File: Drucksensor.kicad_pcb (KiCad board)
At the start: 2 copper layers, 99 x 67 mm, 95 parts, among them J101 Conn_01x02, J102 Start, J103 RJ45, J104 RJ45, J105 DB15_Female_MountingHoles, J106 Serial, J107 Conn_01x03_Male, Q101 Q_NMOS_GSD, Q102 Q_NMOS_GSD, Q103 Q_NMOS_GSD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

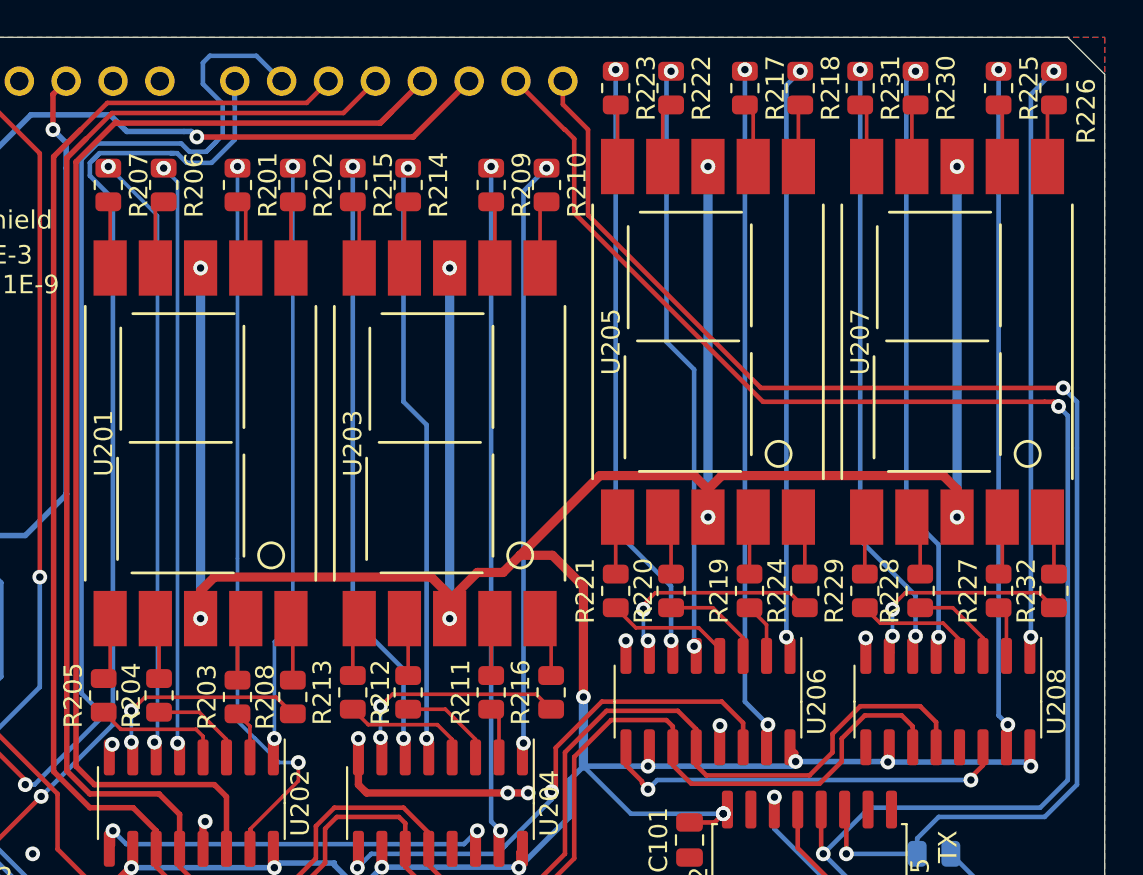
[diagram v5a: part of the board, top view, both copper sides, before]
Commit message: Software-Serial für RS232 interface
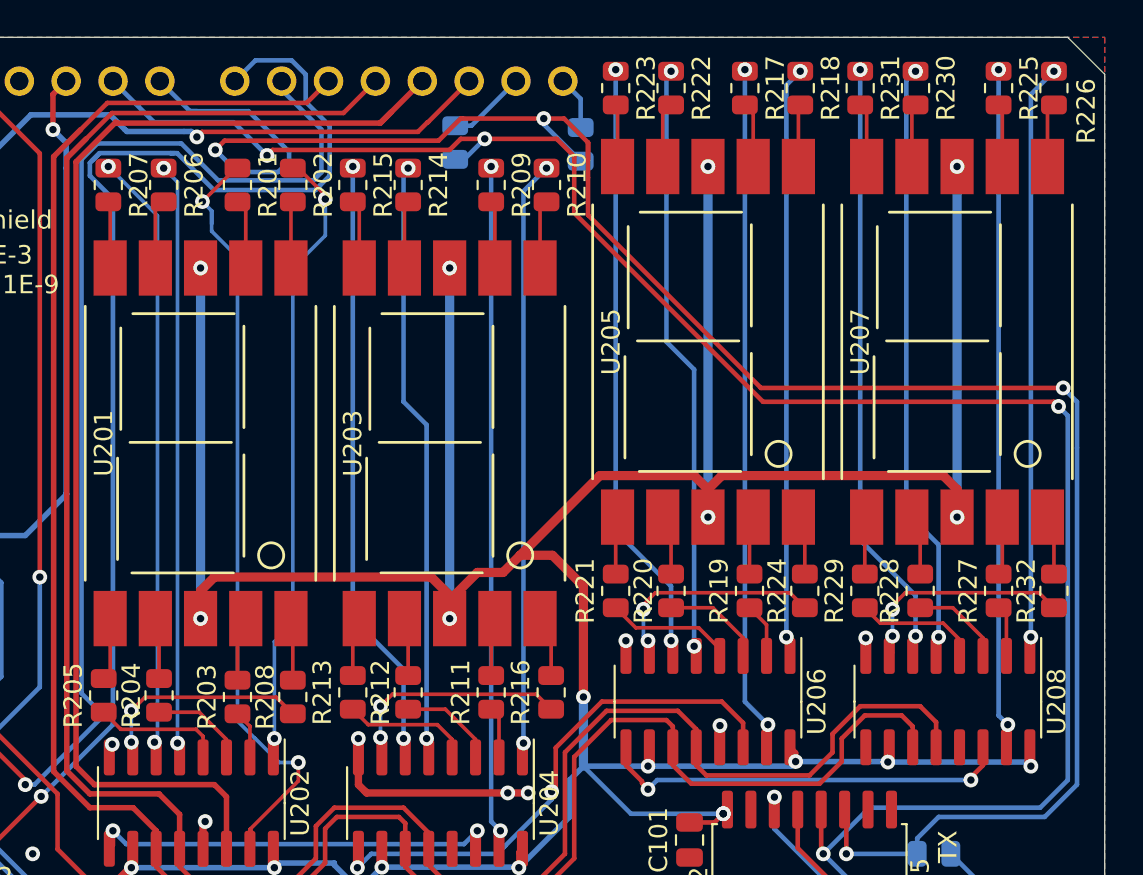
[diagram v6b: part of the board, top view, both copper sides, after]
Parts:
- added R123: Open, Resistor_SMD:R_0805_2012Metric, B.Cu at (119.8, 23.7)
- added R124: Open, Resistor_SMD:R_0805_2012Metric, B.Cu at (126.6, 23.8)
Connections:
- A101 pad 23: unconnected-(A101-Pad23) -> /TX_2
- A101 pad 24: unconnected-(A101-Pad24) -> /RX_2
- R105 pad 2: /TX -> /TX_2
- R116 pad 2: /RX -> /RX_2
- U102 pad 11: /TX -> /TX_2
- U102 pad 12: /RX -> /RX_2
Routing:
- net /TX_2: track 0.00 -> 112.2 mm, vias 0 -> 4
- net /RX_2: track 0.00 -> 107.4 mm, vias 0 -> 4
- net /RX: track 83.3 -> 4.30 mm, vias 2 -> 0
- net /TX: track 76.3 -> 2.92 mm, vias 2 -> 0
- net /Magnetron_Enable: track 61.1 -> 73.2 mm
- net Net-(R201-Pad1): track 41.1 -> 43.4 mm
- net Net-(R202-Pad1): track 32.5 -> 34.2 mm
- net /EnableAll: track 77.7 -> 79.2 mm

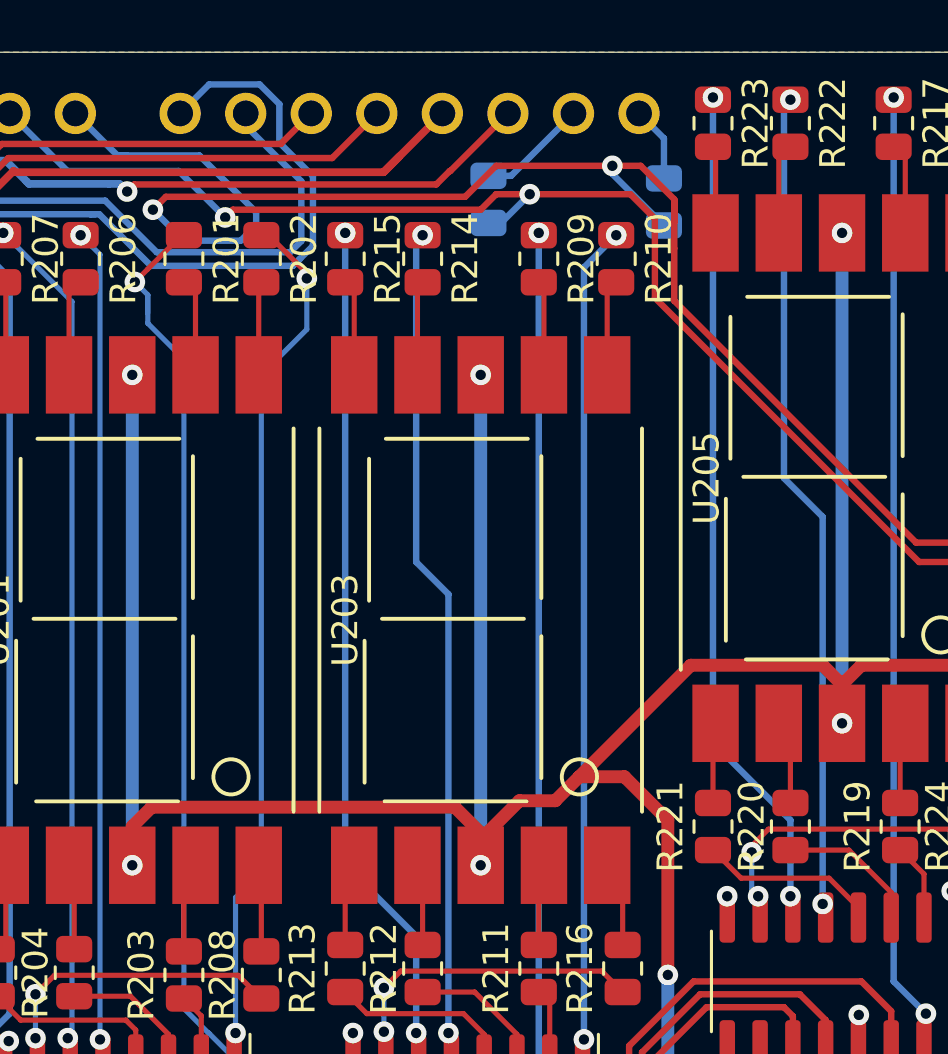
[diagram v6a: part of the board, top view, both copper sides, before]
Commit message: Flächen angepasst
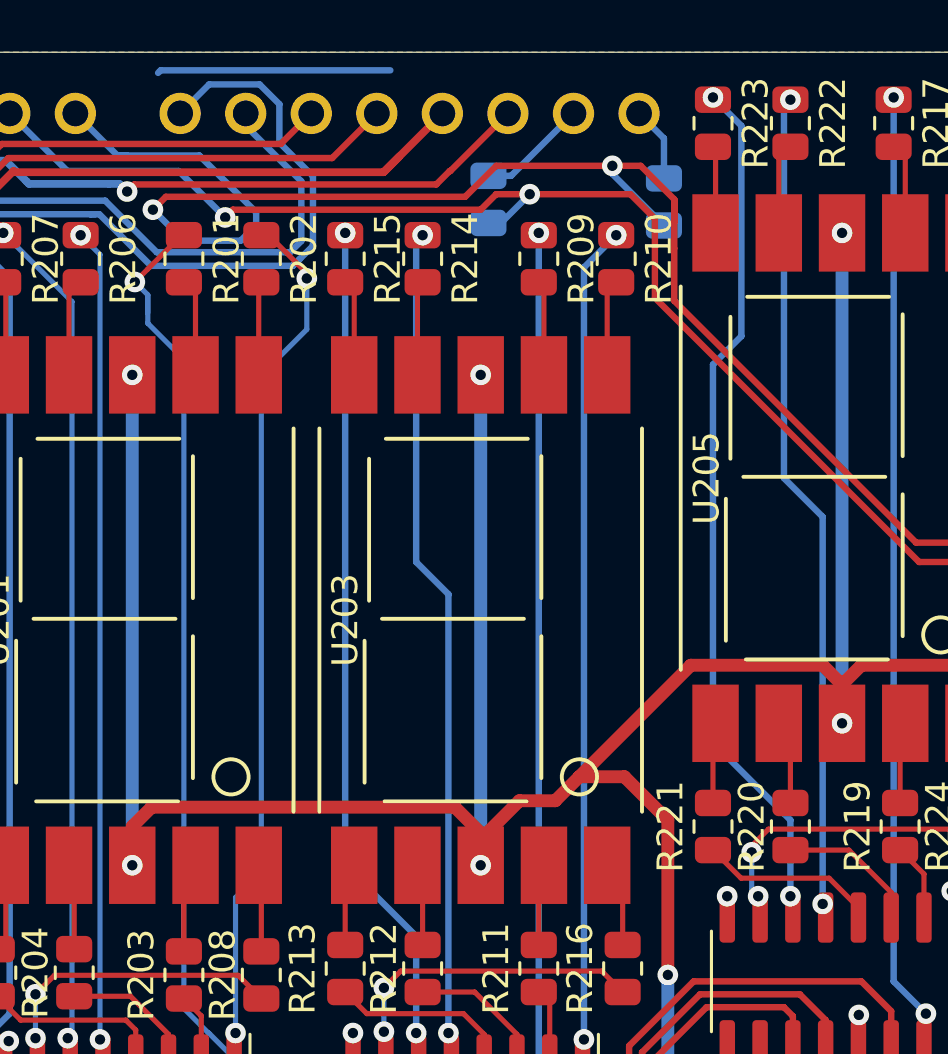
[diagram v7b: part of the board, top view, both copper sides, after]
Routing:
- net GND: track 80.4 -> 89.4 mm
- net Net-(R223-Pad1): track 33.1 -> 34.1 mm
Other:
- board text added: "Bridge for RX/TX_0"
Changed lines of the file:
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@@
     (effects (font (size 2 2) (thickness 0.15)) (justify mirror))
+  )
+  (gr_text "Bridge for RX/TX_0" (at 120.6 26.5) (layer "B.SilkS")
+    (effects (font (size 1 1) (thickness 0.15)) (justify mirror))
   )
   (gr_text "TX RX" (at 154 65.25 90) (layer "B.SilkS")
@@
   (via (at 96.9 62.25) (size 0.8) (drill 0.4) (layers "F.Cu" "B.Cu") (net 12))
   (via (at 82.25 41.25) (size 0.8) (drill 0.4) (layers "F.Cu" "B.Cu") (net 12))
+  (segment (start 116 18.7) (end 107.1 18.7) (width 0.25) (layer "B.Cu") (net 12))
+  (segment (start 107.1 18.7) (end 107 18.8) (width 0.25) (layer "B.Cu") (net 12))
   (segment (start 92.8 63.775) (end 92.8 63.65) (width 0.3) (layer "F.Cu") (net 13))
   (segment (start 94.5 61.95) (end 94.55 61.95) (width 0.25) (layer "F.Cu") (net 13))
@@
   (via (at 128.5 19.75) (size 0.8) (drill 0.4) (layers "F.Cu" "B.Cu") (net 80))
   (via (at 131.5 50.6995) (size 0.8) (drill 0.4) (layers "F.Cu" "B.Cu") (net 80))
-  (segment (start 128.5 19.75) (end 128.5 44.75) (width 0.25) (layer "B.Cu") (net 80))
-  (segment (start 131.5 47.75) (end 131.5 50.6995) (width 0.25) (layer "B.Cu") (net 80))
-  (segment (start 128.5 44.75) (end 131.5 47.75) (width 0.25) (layer "B.Cu") (net 80))
+  (segment (start 129.6 29) (end 129.6 20.85) (width 0.25) (layer "B.Cu") (net 80))
+  (segment (start 129.6 20.85) (end 128.5 19.75) (width 0.25) (layer "B.Cu") (net 80))
+  (segment (start 128.5 44.75) (end 128.5 30.1) (width 0.25) (layer "B.Cu") (net 80))
+  (segment (start 131.5 47.75) (end 128.5 44.75) (width 0.25) (layer "B.Cu") (net 80))
+  (segment (start 131.5 50.6995) (end 131.5 47.75) (width 0.25) (layer "B.Cu") (net 80))
+  (segment (start 128.5 30.1) (end 129.6 29) (width 0.25) (layer "B.Cu") (net 80))
   (segment (start 128.6 21.7625) (end 128.5 21.6625) (width 0.2) (layer "F.Cu") (net 81))
   (segment (start 128.6 25) (end 128.6 21.7625) (width 0.2) (layer "F.Cu") (net 81))

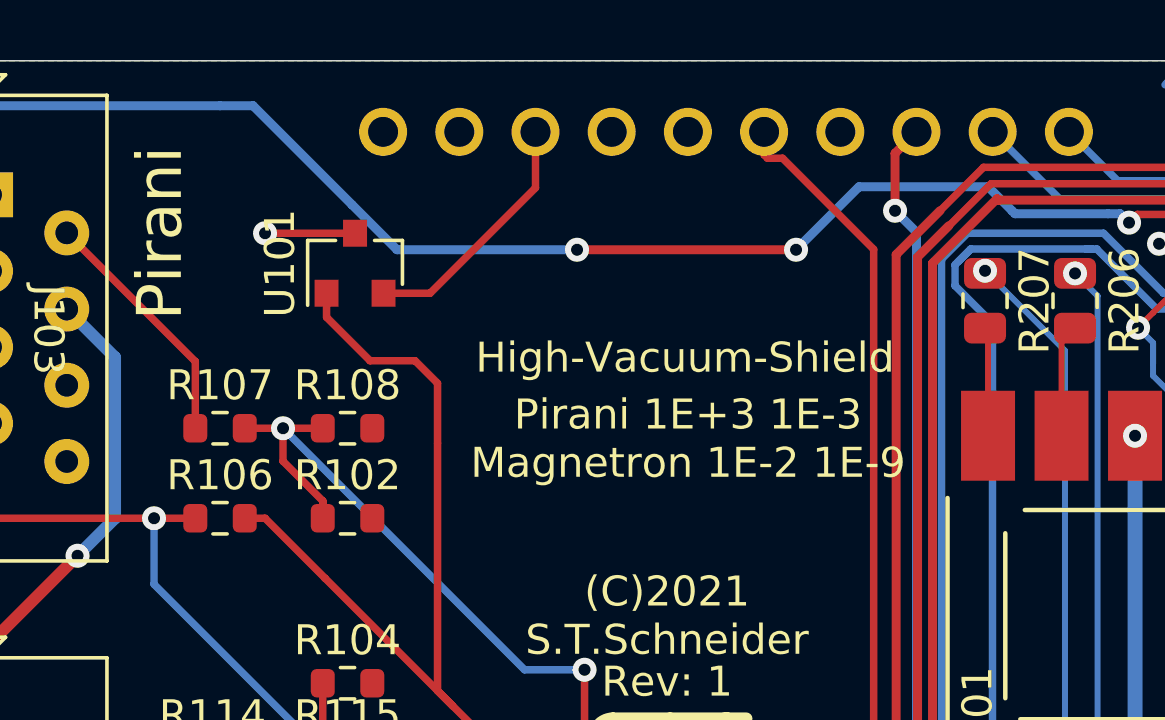
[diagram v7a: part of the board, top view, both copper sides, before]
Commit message: Kondensatoren für V-Ref
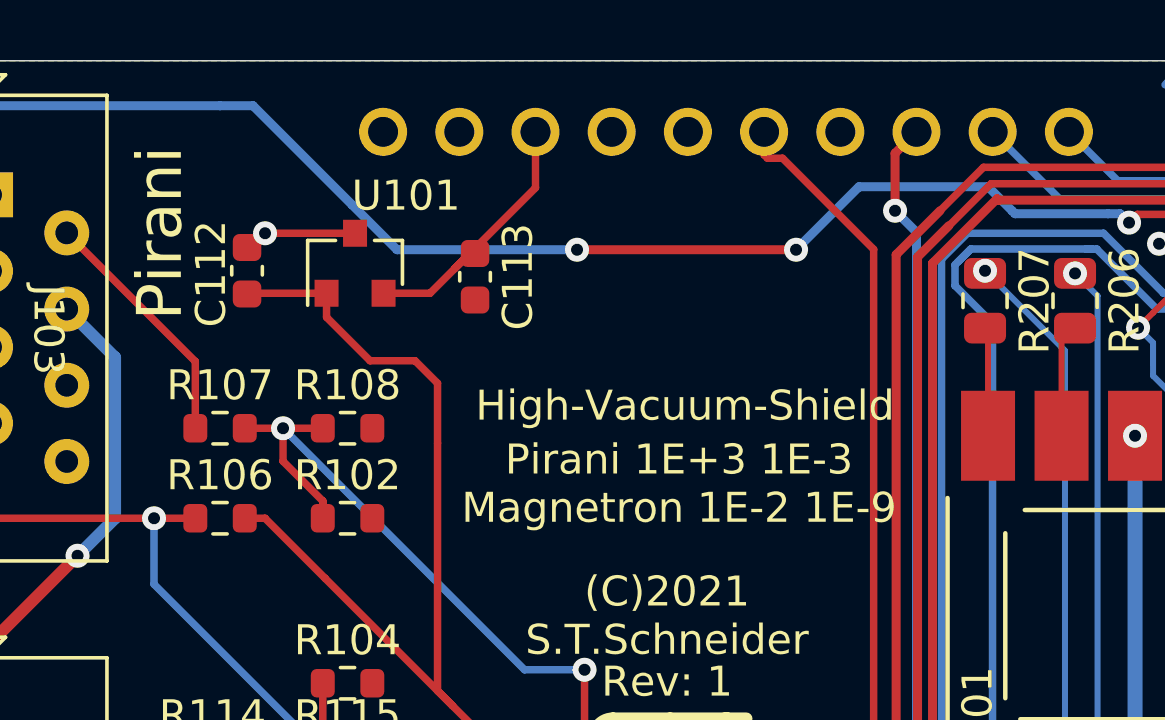
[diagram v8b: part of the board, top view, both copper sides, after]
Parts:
- added C112: 100n, Capacitor_SMD:C_0603_1608Metric, F.Cu at (76.4, 25.0)
- added C113: 100n, Capacitor_SMD:C_0603_1608Metric, F.Cu at (84.0, 25.2)
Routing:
- net +5V: track 298.6 -> 301.2 mm
- net Net-(A101-Pad30): track 8.39 -> 9.27 mm
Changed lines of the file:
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@@
     )
   )
+  (footprint "Capacitor_SMD:C_0603_1608Metric" (layer "F.Cu")
+    (at 84 25.2 -90)
+    (descr "Capacitor SMD 0603 (1608 Metric), square (rectangular) end terminal, IPC_7351 nominal, (Body size source: IPC-SM-782 page 76, https://www.pcb-3d.com/wordpress/wp-content/uploads/ipc-sm-782a_amendment_1_and_2.pdf), generated with kicad-footprint-generator")
+    (tags "capacitor")
+    (property "Sheetfile" "Drucksensor.kicad_sch")
+    (property "Sheetname" "")
+    (attr smd)
+    (fp_text reference "C113" (at 0 -1.43 90) (layer "F.SilkS")
+      (effects (font (size 1 1) (thickness 0.15)))
+    )
+    (fp_text value "100n" (at 0 1.43 90) (layer "F.Fab")
+      (effects (font (size 1 1) (thickness 0.15)))
+    )
+    (fp_text user "${REFERENCE}" (at 0 0 90) (layer "F.Fab")
+      (effects (font (size 0.4 0.4) (thickness 0.06)))
+    )
+    (fp_line (start -0.14058 0.51) (end 0.14058 0.51) (layer "F.SilkS") (width 0.12))
+    (fp_line (start -0.14058 -0.51) (end 0.14058 -0.51) (layer "F.SilkS") (width 0.12))
+    (fp_line (start 1.48 -0.73) (end 1.48 0.73) (layer "F.CrtYd") (width 0.05))
+    (fp_line (start -1.48 -0.73) (end 1.48 -0.73) (layer "F.CrtYd") (width 0.05))
+    (fp_line (start 1.48 0.73) (end -1.48 0.73) (layer "F.CrtYd") (width 0.05))
+    (fp_line (start -1.48 0.73) (end -1.48 -0.73) (layer "F.CrtYd") (width 0.05))
+    (fp_line (start -0.8 0.4) (end -0.8 -0.4) (layer "F.Fab") (width 0.1))
+    (fp_line (start 0.8 0.4) (end -0.8 0.4) (layer "F.Fab") (width 0.1))
+    (fp_line (start 0.8 -0.4) (end 0.8 0.4) (layer "F.Fab") (width 0.1))
+    (fp_line (start -0.8 -0.4) (end 0.8 -0.4) (layer "F.Fab") (width 0.1))
+    (pad "1" smd roundrect locked (at -0.775 0 270) (size 0.9 0.95) (layers "F.Cu" "F.Paste" "F.Mask") (roundrect_rratio 0.25)
+      (net 26 "Net-(A101-Pad30)") (pintype "passive"))
+    (pad "2" smd roundrect locked (at 0.775 0 270) (size 0.9 0.95) (layers "F.Cu" "F.Paste" "F.Mask") (roundrect_rratio 0.25)
+      (net 12 "GND") (pintype "passive"))
+    (model "${KISYS3DMOD}/Capacitor_SMD.3dshapes/C_0603_1608Metric.wrl"
+      (offset (xyz 0 0 0))
+      (scale (xyz 1 1 1))
+      (rotate (xyz 0 0 0))
+    )
+  )
   (footprint "Resistor_SMD:R_1210_3225Metric" (layer "F.Cu")
     (at 64 75 -90)
@@
     )
   )
+  (footprint "Capacitor_SMD:C_0603_1608Metric" (layer "F.Cu")
+    (at 76.4 25 -90)
+    (descr "Capacitor SMD 0603 (1608 Metric), square (rectangular) end terminal, IPC_7351 nominal, (Body size source: IPC-SM-782 page 76, https://www.pcb-3d.com/wordpress/wp-content/uploads/ipc-sm-782a_amendment_1_and_2.pdf), generated with kicad-footprint-generator")
+    (tags "capacitor")
+    (property "Sheetfile" "Drucksensor.kicad_sch")
+    (property "Sheetname" "")
+    (attr smd)
+    (fp_text reference "C112" (at 0.1 1.2 -90) (layer "F.SilkS")
+      (effects (font (size 1 1) (thickness 0.15)))
+    )
+    (fp_text value "100n" (at 0 1.43 90) (layer "F.Fab")
+      (effects (font (size 1 1) (thickness 0.15)))
+    )
+    (fp_text user "${REFERENCE}" (at 0 0 90) (layer "F.Fab")
+      (effects (font (size 0.4 0.4) (thickness 0.06)))
+    )
+    (fp_line (start -0.14058 -0.51) (end 0.14058 -0.51) (layer "F.SilkS") (width 0.12))
+    (fp_line (start -0.14058 0.51) (end 0.14058 0.51) (layer "F.SilkS") (width 0.12))
+    (fp_line (start 1.48 0.73) (end -1.48 0.73) (layer "F.CrtYd") (width 0.05))
+    (fp_line (start -1.48 0.73) (end -1.48 -0.73) (layer "F.CrtYd") (width 0.05))
+    (fp_line (start 1.48 -0.73) (end 1.48 0.73) (layer "F.CrtYd") (width 0.05))
+    (fp_line (start -1.48 -0.73) (end 1.48 -0.73) (layer "F.CrtYd") (width 0.05))
+    (fp_line (start 0.8 -0.4) (end 0.8 0.4) (layer "F.Fab") (width 0.1))
+    (fp_line (start 0.8 0.4) (end -0.8 0.4) (layer "F.Fab") (width 0.1))
+    (fp_line (start -0.8 -0.4) (end 0.8 -0.4) (layer "F.Fab") (width 0.1))
+    (fp_line (start -0.8 0.4) (end -0.8 -0.4) (layer "F.Fab") (width 0.1))
+    (pad "1" smd roundrect locked (at -0.775 0 270) (size 0.9 0.95) (layers "F.Cu" "F.Paste" "F.Mask") (roundrect_rratio 0.25)
+      (net 12 "GND") (pintype "passive"))
+    (pad "2" smd roundrect locked (at 0.775 0 270) (size 0.9 0.95) (layers "F.Cu" "F.Paste" "F.Mask") (roundrect_rratio 0.25)
+      (net 28 "+5V") (pintype "passive"))
+    (model "${KISYS3DMOD}/Capacitor_SMD.3dshapes/C_0603_1608Metric.wrl"
+      (offset (xyz 0 0 0))
+      (scale (xyz 1 1 1))
+      (rotate (xyz 0 0 0))
+    )
+  )
   (footprint "Resistor_SMD:R_0805_2012Metric" (layer "F.Cu")
     (at 121.75 26 -90)
@@
     (property "Sheetname" "")
     (attr smd)
-    (fp_text reference "U101" (at 0 -2.5 90) (layer "F.SilkS")
+    (fp_text reference "U101" (at 2.25 1.7 180) (layer "F.SilkS")
       (effects (font (size 1 1) (thickness 0.15)))
     )
@@
     (effects (font (size 1 1) (thickness 0.15)))
   )
-  (gr_text "Pirani 1E+3 1E-3\nMagnetron 1E-2 1E-9" (at 91.1 30.6) (layer "F.SilkS")
+  (gr_text "Pirani 1E+3 1E-3\nMagnetron 1E-2 1E-9" (at 90.8 32.1) (layer "F.SilkS")
     (effects (font (size 1 1) (thickness 0.15)))
   )
@@
     (effects (font (size 1 1) (thickness 0.15)))
   )
-  (gr_text "High-Vacuum-Shield\n" (at 91 27.9) (layer "F.SilkS")
+  (gr_text "High-Vacuum-Shield\n" (at 91 29.5) (layer "F.SilkS")
     (effects (font (size 1 1) (thickness 0.15)))
   )
@@
   (segment (start 128 71.175) (end 125 71.175) (width 0.25) (layer "F.Cu") (net 25))
   (segment (start 125 69.265) (end 125.635 68.63) (width 0.25) (layer "F.Cu") (net 25))
-  (segment (start 82.5 25.75) (end 86.015 22.235) (width 0.25) (layer "F.Cu") (net 26))
+  (segment (start 83.325 24.925) (end 86.015 22.235) (width 0.25) (layer "F.Cu") (net 26))
   (segment (start 86.015 22.235) (end 86.015 20.37) (width 0.25) (layer "F.Cu") (net 26))
   (segment (start 80.95 25.75) (end 82.5 25.75) (width 0.25) (layer "F.Cu") (net 26))
+  (segment (start 83.825 24.425) (end 83.325 24.925) (width 0.25) (layer "F.Cu") (net 26))
+  (segment (start 82.5 25.75) (end 83.325 24.925) (width 0.25) (layer "F.Cu") (net 26))
+  (segment (start 84 24.425) (end 83.825 24.425) (width 0.25) (layer "F.Cu") (net 26))
   (segment (start 84.25 67) (end 87.75 63.5) (width 0.3) (layer "F.Cu") (net 27))
   (segment (start 70 66.535) (end 70 57) (width 0.4) (layer "F.Cu") (net 27))
@@
   (segment (start 134.555 59.85) (end 134.3275 60.0775) (width 0.25) (layer "F.Cu") (net 28))
   (segment (start 98.25 59) (end 98.25 62) (width 0.25) (layer "F.Cu") (net 28))
+  (segment (start 76.425 25.75) (end 76.4 25.775) (width 0.25) (layer "F.Cu") (net 28))
   (segment (start 118.5 47.25) (end 106.75 47.25) (width 0.5) (layer "F.Cu") (net 28))
   (segment (start 121 47) (end 119.5 48.5) (width 0.5) (layer "F.Cu") (net 28))
@@
   (segment (start 86.25 46.925) (end 85.325 46) (width 0.25) (layer "F.Cu") (net 28))
   (segment (start 143.25 57.2755) (end 143.25 56.55) (width 0.3) (layer "F.Cu") (net 28))
+  (segment (start 79.05 25.75) (end 76.425 25.75) (width 0.25) (layer "F.Cu") (net 28))
   (segment (start 138.25 56.78) (end 137.945 56.475) (width 0.3) (layer "F.Cu") (net 28))
   (segment (start 100.235 63.985) (end 100.235 65.015) (width 0.25) (layer "F.Cu") (net 28))
